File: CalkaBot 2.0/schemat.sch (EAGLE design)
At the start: 53 parts, among them IC1 TB6612FNG, IC2 LM339D, IC3 7806DT, Q1 16MHz

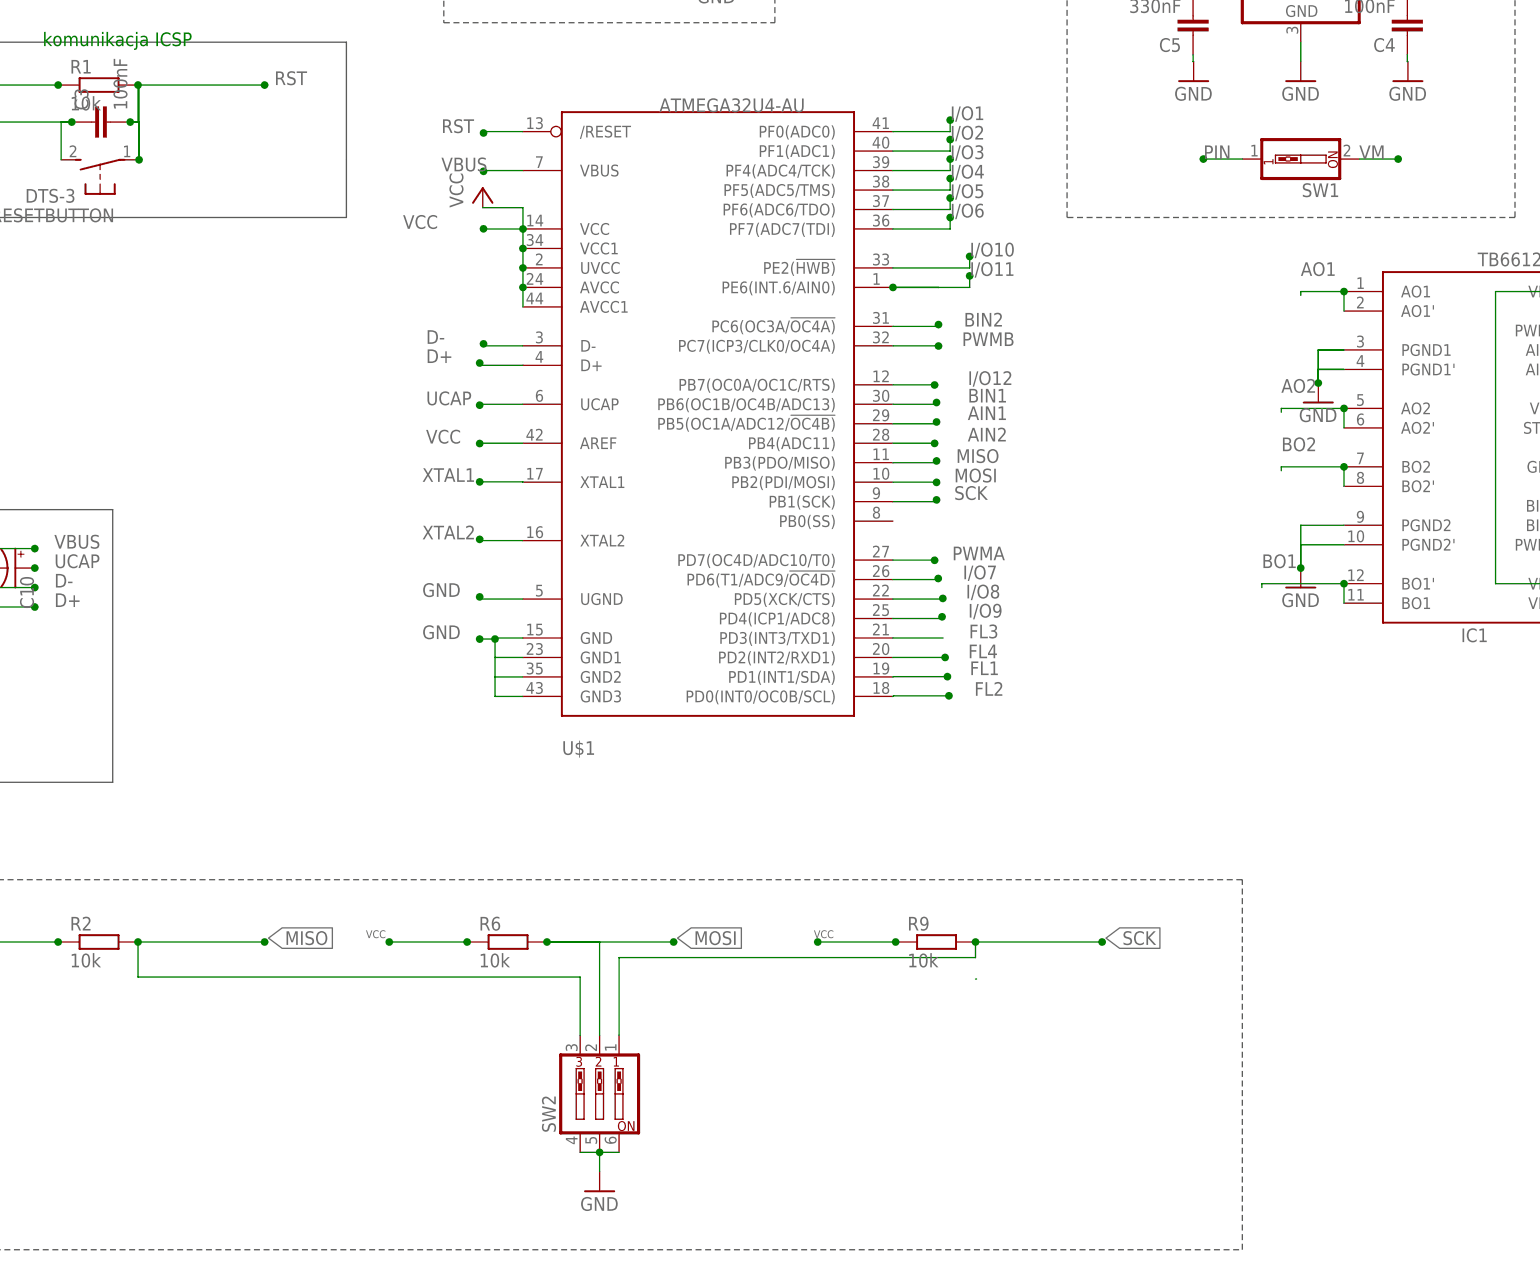
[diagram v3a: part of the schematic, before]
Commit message: poprawki wprowadzone, zmiana dipa z 3 na 4, przesunięcie włącznika zasilania
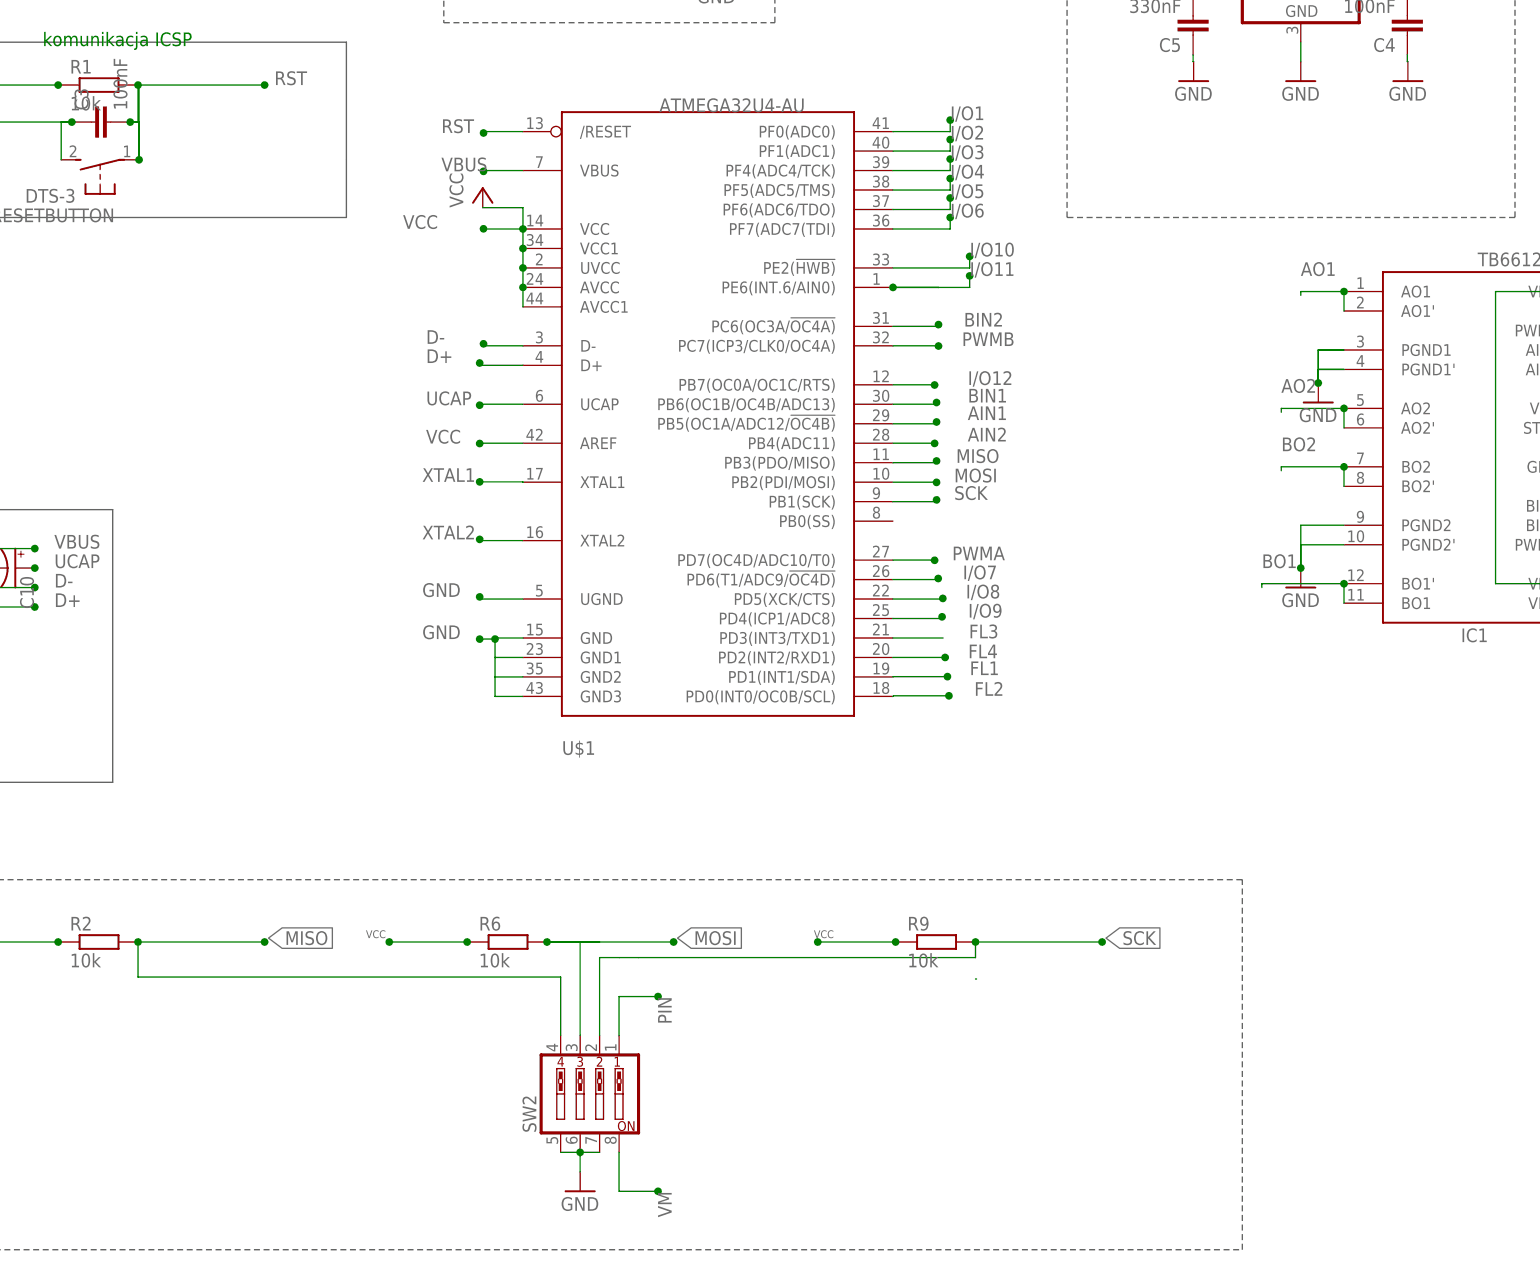
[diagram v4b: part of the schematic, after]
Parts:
- removed SW1: (no value), special:SW_DIP-1
- SW2: device special:SW_DIP-3 -> special:SW_DIP-4
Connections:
- net GND: now also SW2.7; no longer SW2.4
- net MISO: now also SW2.4; no longer SW2.3
- net MOSI: now also SW2.3; no longer SW2.2
- net PIN: now also SW2.1; no longer SW1.1
- net SCK: now also SW2.2; no longer SW2.1
- net VM: now also SW2.8; no longer SW1.2
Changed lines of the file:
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@@
 <part name="C10" library="rcl" library_urn="urn:adsk.eagle:library:334" deviceset="CPOL-US" device="UD-4X5,8" package3d_urn="urn:adsk.eagle:package:23474/1" value="1uF"/>
 <part name="GND21" library="supply1" library_urn="urn:adsk.eagle:library:371" deviceset="GND" device=""/>
-<part name="SW1" library="special" library_urn="urn:adsk.eagle:library:367" deviceset="SW_DIP-1" device="" package3d_urn="urn:adsk.eagle:package:26661/1"/>
 <part name="JP2" library="pinhead" library_urn="urn:adsk.eagle:library:325" deviceset="PINHD-1X5" device="" package3d_urn="urn:adsk.eagle:package:22469/2"/>
-<part name="SW2" library="special" library_urn="urn:adsk.eagle:library:367" deviceset="SW_DIP-3" device="" package3d_urn="urn:adsk.eagle:package:26663/2"/>
+<part name="SW2" library="special" library_urn="urn:adsk.eagle:library:367" deviceset="SW_DIP-4" device="" package3d_urn="urn:adsk.eagle:package:26655/2"/>
 <part name="GND22" library="supply1" library_urn="urn:adsk.eagle:library:371" deviceset="GND" device=""/>
 <part name="R23" library="rcl" library_urn="urn:adsk.eagle:library:334" deviceset="R-EU_" device="R0805" package3d_urn="urn:adsk.eagle:package:23553/2" value="220R"/>
@@
 <attribute name="VALUE" x="-106.68" y="33.02" size="1.778" layer="96"/>
 </instance>
-<instance part="SW1" gate="G$1" x="68.58" y="101.6" smashed="yes" rot="R180">
-<attribute name="NAME" x="73.66" y="98.425" size="1.778" layer="95" rot="R180"/>
-<attribute name="VALUE" x="73.66" y="106.68" size="1.778" layer="96" rot="R180"/>
-</instance>
 <instance part="JP2" gate="A" x="-119.38" y="25.4" smashed="yes" rot="R270">
 <attribute name="NAME" x="-111.125" y="31.75" size="1.778" layer="95" rot="R270"/>
 <attribute name="VALUE" x="-129.54" y="31.75" size="1.778" layer="96" rot="R270"/>
 </instance>
-<instance part="SW2" gate="A" x="-22.86" y="-20.32" smashed="yes" rot="R90">
-<attribute name="NAME" x="-28.575" y="-25.4" size="1.778" layer="95" rot="R90"/>
-<attribute name="VALUE" x="-15.24" y="-25.4" size="1.778" layer="96" rot="R90"/>
-</instance>
-<instance part="GND22" gate="1" x="-22.86" y="-33.02" smashed="yes">
-<attribute name="VALUE" x="-25.4" y="-35.56" size="1.778" layer="96"/>
+<instance part="SW2" gate="A" x="-25.4" y="-20.32" smashed="yes" rot="R90">
+<attribute name="NAME" x="-31.115" y="-25.4" size="1.778" layer="95" rot="R90"/>
+<attribute name="VALUE" x="-17.78" y="-25.4" size="1.778" layer="96" rot="R90"/>
+</instance>
+<instance part="GND22" gate="1" x="-25.4" y="-33.02" smashed="yes">
+<attribute name="VALUE" x="-27.94" y="-35.56" size="1.778" layer="96"/>
 </instance>
 <instance part="R23" gate="G$1" x="-25.062" y="131.508" smashed="yes" rot="R180">
@@
 </segment>
 <segment>
-<pinref part="SW2" gate="A" pin="4"/>
-<pinref part="SW2" gate="A" pin="5"/>
-<wire x1="-25.4" y1="-27.94" x2="-22.86" y2="-27.94" width="0.1524" layer="91"/>
-<pinref part="SW2" gate="A" pin="6"/>
-<wire x1="-22.86" y1="-27.94" x2="-20.32" y2="-27.94" width="0.1524" layer="91"/>
-<junction x="-22.86" y="-27.94"/>
-<wire x1="-22.86" y1="-27.94" x2="-22.86" y2="-30.48" width="0.1524" layer="91"/>
-<pinref part="GND22" gate="1" pin="GND"/>
-</segment>
-<segment>
 <pinref part="JP2" gate="A" pin="2"/>
 <wire x1="-116.84" y1="40.64" x2="-116.84" y2="27.94" width="0.1524" layer="91"/>
@@
 <wire x1="-7.62" y1="131.56" x2="-7.62" y2="127" width="0.1524" layer="91"/>
 </segment>
+<segment>
+<pinref part="SW2" gate="A" pin="5"/>
+<pinref part="SW2" gate="A" pin="6"/>
+<wire x1="-27.94" y1="-27.94" x2="-25.4" y2="-27.94" width="0.1524" layer="91"/>
+<pinref part="SW2" gate="A" pin="7"/>
+<wire x1="-22.86" y1="-27.94" x2="-25.4" y2="-27.94" width="0.1524" layer="91"/>
+<junction x="-25.4" y="-27.94"/>
+<pinref part="GND22" gate="1" pin="GND"/>
+<wire x1="-25.4" y1="-27.94" x2="-25.4" y2="-30.48" width="0.1524" layer="91"/>
+</segment>
 </net>
 <net name="D-" class="0">
@@
 <label x="-66.04" y="0" size="1.778" layer="95" xref="yes"/>
 <wire x1="-83.058" y1="-0.508" x2="-83.058" y2="-5.08" width="0.1524" layer="91"/>
-<wire x1="-83.058" y1="-5.08" x2="-25.4" y2="-5.08" width="0.1524" layer="91"/>
+<wire x1="-83.058" y1="-5.08" x2="-27.94" y2="-5.08" width="0.1524" layer="91"/>
 <junction x="-83.058" y="-0.508"/>
-<pinref part="SW2" gate="A" pin="3"/>
-<wire x1="-25.4" y1="-5.08" x2="-25.4" y2="-12.7" width="0.1524" layer="91"/>
+<pinref part="SW2" gate="A" pin="4"/>
+<wire x1="-27.94" y1="-5.08" x2="-27.94" y2="-12.7" width="0.1524" layer="91"/>
 </segment>
 </net>
@@
 <junction x="-13.208" y="-0.508"/>
 <label x="-12.7" y="0" size="1.778" layer="95" xref="yes"/>
-<pinref part="SW2" gate="A" pin="2"/>
 <wire x1="-29.718" y1="-0.508" x2="-22.86" y2="-0.508" width="0.1524" layer="91"/>
-<wire x1="-22.86" y1="-0.508" x2="-22.86" y2="-12.7" width="0.1524" layer="91"/>
 <junction x="-29.718" y="-0.508"/>
+<pinref part="SW2" gate="A" pin="3"/>
+<wire x1="-25.4" y1="-12.7" x2="-25.4" y2="-0.508" width="0.1524" layer="91"/>
+<wire x1="-25.4" y1="-0.508" x2="-29.718" y2="-0.508" width="0.1524" layer="91"/>
 </segment>
 </net>
@@
 <wire x1="26.162" y1="-0.508" x2="26.162" y2="-2.54" width="0.1524" layer="91"/>
 <junction x="26.162" y="-0.508"/>
-<pinref part="SW2" gate="A" pin="1"/>
-<wire x1="26.162" y1="-2.54" x2="-20.32" y2="-2.54" width="0.1524" layer="91"/>
-<wire x1="-20.32" y1="-2.54" x2="-20.32" y2="-12.7" width="0.1524" layer="91"/>
+<wire x1="26.162" y1="-2.54" x2="-17.78" y2="-2.54" width="0.1524" layer="91"/>
+<pinref part="SW2" gate="A" pin="2"/>
+<wire x1="-17.78" y1="-2.54" x2="-20.32" y2="-2.54" width="0.1524" layer="91"/>
+<wire x1="-22.86" y1="-12.7" x2="-22.86" y2="-2.54" width="0.1524" layer="91"/>
+<wire x1="-22.86" y1="-2.54" x2="-20.32" y2="-2.54" width="0.1524" layer="91"/>
 </segment>
 </net>
@@
 </segment>
 <segment>
-<pinref part="SW1" gate="G$1" pin="2"/>
-<wire x1="76.2" y1="101.6" x2="81.28" y2="101.6" width="0.1524" layer="91"/>
-<junction x="81.28" y="101.6"/>
-<label x="76.2" y="101.6" size="1.778" layer="95"/>
+<label x="-15.24" y="-33.02" size="1.778" layer="95" rot="R270"/>
+<pinref part="SW2" gate="A" pin="8"/>
+<wire x1="-15.24" y1="-33.02" x2="-20.32" y2="-33.02" width="0.1524" layer="91"/>
+<wire x1="-20.32" y1="-33.02" x2="-20.32" y2="-27.94" width="0.1524" layer="91"/>
+<junction x="-15.24" y="-33.02"/>
 </segment>
 </net>
@@
 </segment>
 <segment>
-<pinref part="SW1" gate="G$1" pin="1"/>
-<wire x1="60.96" y1="101.6" x2="55.88" y2="101.6" width="0.1524" layer="91"/>
-<junction x="55.88" y="101.6"/>
-<label x="55.88" y="101.6" size="1.778" layer="95"/>
-</segment>
-</net>
+<label x="-15.24" y="-7.62" size="1.778" layer="95" rot="R270"/>
+<pinref part="SW2" gate="A" pin="1"/>
+<wire x1="-15.24" y1="-7.62" x2="-20.32" y2="-7.62" width="0.1524" layer="91"/>
+<wire x1="-20.32" y1="-7.62" x2="-20.32" y2="-12.7" width="0.1524" layer="91"/>
+<junction x="-15.24" y="-7.62"/>
+</segment>
+</net>
